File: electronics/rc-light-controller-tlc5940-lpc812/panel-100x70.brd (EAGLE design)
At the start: 100 x 70 mm, 120 parts, among them U1 TLC5940PWP, U2 TLC5940PWP, U3 TLC5940PWP

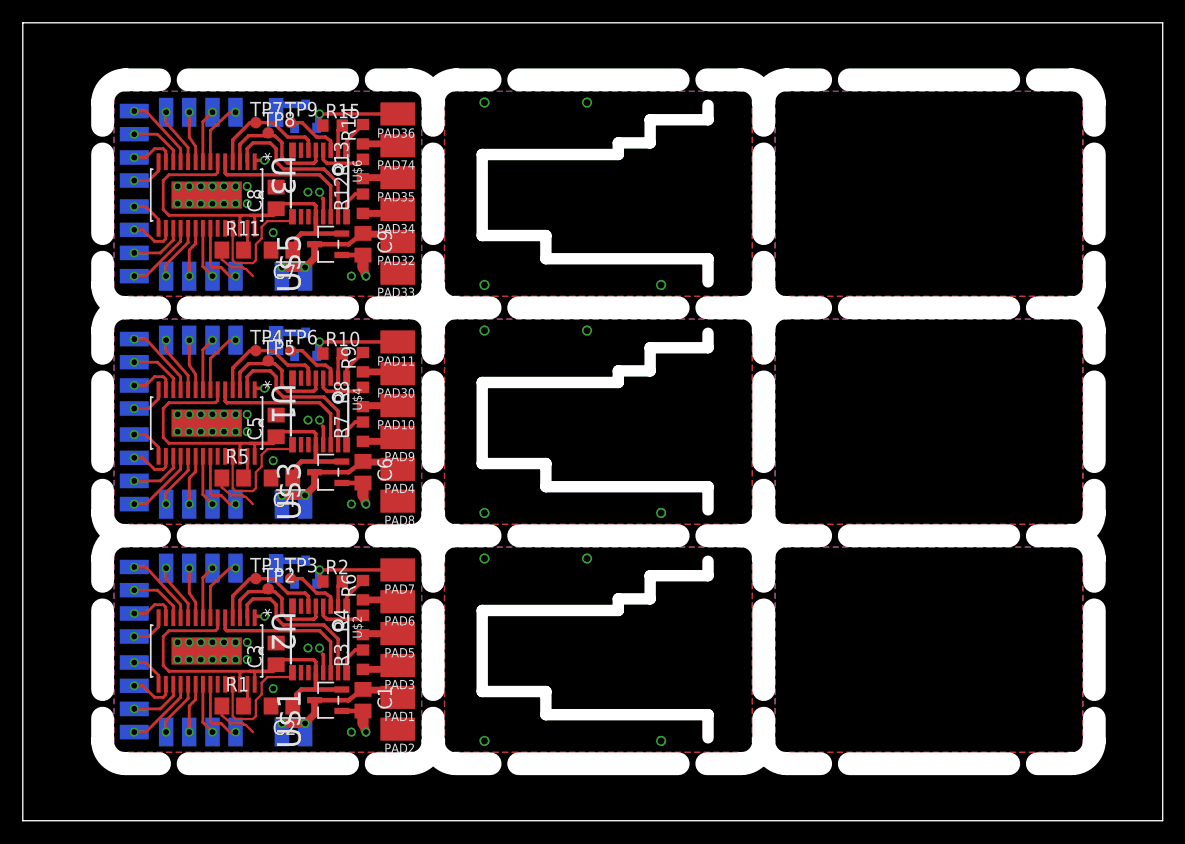
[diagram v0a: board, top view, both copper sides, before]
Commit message: Fix small issues and make new panel
Looks to be ready for PCB making!
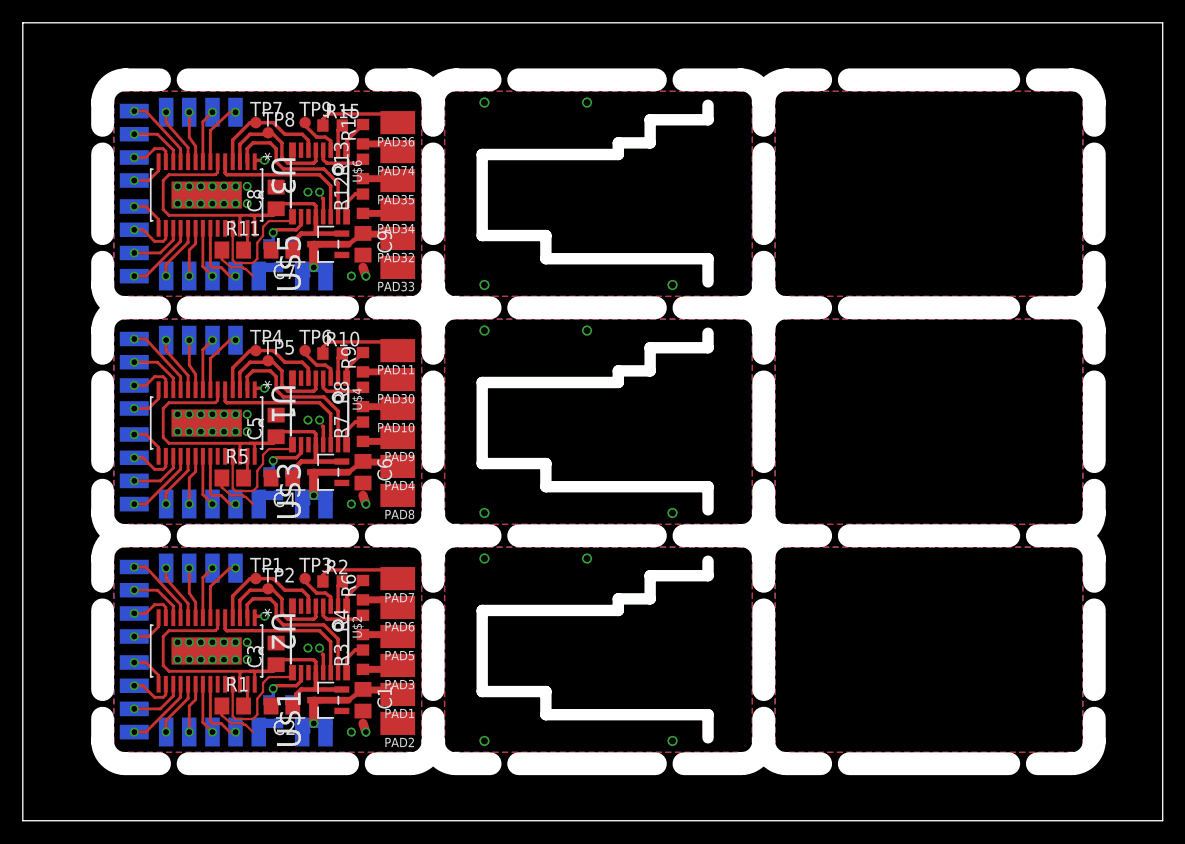
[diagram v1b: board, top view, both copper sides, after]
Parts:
- moved PAD70 14.4 mm to (20.7, 7.78)
- moved PAD31 14.4 mm to (20.7, 27.8)
- moved PAD75 14.4 mm to (20.7, 47.8)
- moved T1 12.5 mm to (22.5, 9.56), turned to 0 degrees
- moved T3 12.5 mm to (22.5, 49.6), turned to 0 degrees
- moved T2 12.5 mm to (22.5, 29.6), turned to 0 degrees
- moved PAD28 3.81 mm to (26.5, 27.8)
- moved PAD67 3.81 mm to (26.5, 7.78)
- moved PAD72 3.81 mm to (26.5, 47.8)
- moved TP3 1.27 mm to (24.8, 21.2)
- moved TP6 1.27 mm to (24.8, 41.2)
- moved TP9 1.27 mm to (24.8, 61.2)
- moved PAD11 0.76 mm to (32.9, 41.2)
- moved PAD36 0.76 mm to (32.9, 61.2)
- moved PAD7 0.76 mm to (32.9, 21.2)
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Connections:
- removed net GND: C1.2, C2.2, C3.2, PAD2.1, R1.1, T1.2, U$1.1, U$2.13, U2.1, U2.29
- removed net GND1: C4.2, C5.2, C6.2, PAD8.1, R5.1, T2.2, U$3.1, U$4.13, U1.1, U1.29
- removed net N$2 (its old number): PAD7.1, R2.1, T1.3
- new net GND3: C1.2, C2.2, C3.2, PAD2.1, R1.1, T1.2, U$1.1, U$2.13, U2.1, U2.29
- new net GND5: C7.2, C8.2, C9.2, PAD33.1, R11.1, T3.2, U$5.1, U$6.13, U3.1, U3.29
- new net N$5: PAD7.1, R2.1
- new net OUT-SWITCHED: T1.3, U$2.10
- new net OUT-SWITCHED1: T2.3, U$4.10
- new net OUT-SWITCHED2: T3.3, U$6.10
- net GND4: now also C4.2, C5.2, C6.2, PAD8.1, R5.1, T2.2, U$3.1, U$4.13, U1.1, U1.29; no longer C7.2, C8.2, C9.2, PAD33.1, R11.1, T3.2, U$5.1, U$6.13, U3.1, U3.29
- net N$10: no longer T2.3
- net N$16: no longer T3.3
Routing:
- net GND1: track 11.4 -> 0.00 mm, vias 20 -> 4
- net GND: track 11.4 -> 0.00 mm, vias 20 -> 4
- net N$2 (its old number): track 10.2 -> 0.00 mm, vias 1 -> 0
- net GND5: track 0.00 -> 8.51 mm, vias 4 -> 19
- net GND3: track 0.00 -> 8.51 mm, vias 4 -> 19
- net N$5: track 0.00 -> 7.62 mm
- net OUT-SWITCHED: track 0.00 -> 4.80 mm, vias 0 -> 1
- net OUT-SWITCHED1: track 0.00 -> 4.80 mm, vias 0 -> 1
- net OUT-SWITCHED2: track 0.00 -> 4.80 mm, vias 0 -> 1
- net VIN2: track 17.9 -> 14.9 mm, vias 2 -> 1
- net VIN1: track 17.9 -> 14.9 mm, vias 2 -> 1
- net VIN: track 17.9 -> 14.9 mm, vias 2 -> 1
- net GND4: track 11.4 -> 8.51 mm, vias 20 -> 19
- net N$16: track 10.2 -> 7.62 mm, vias 1 -> 0
- net N$10: track 10.2 -> 7.62 mm, vias 1 -> 0
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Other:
- outline, holes or cut-outs redrawn
